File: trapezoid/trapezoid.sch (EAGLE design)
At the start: 33 parts, among them U1 MMA8452Q, U2 microSD, U4 MCP73831, Y1 CRYSTAL.ABS25

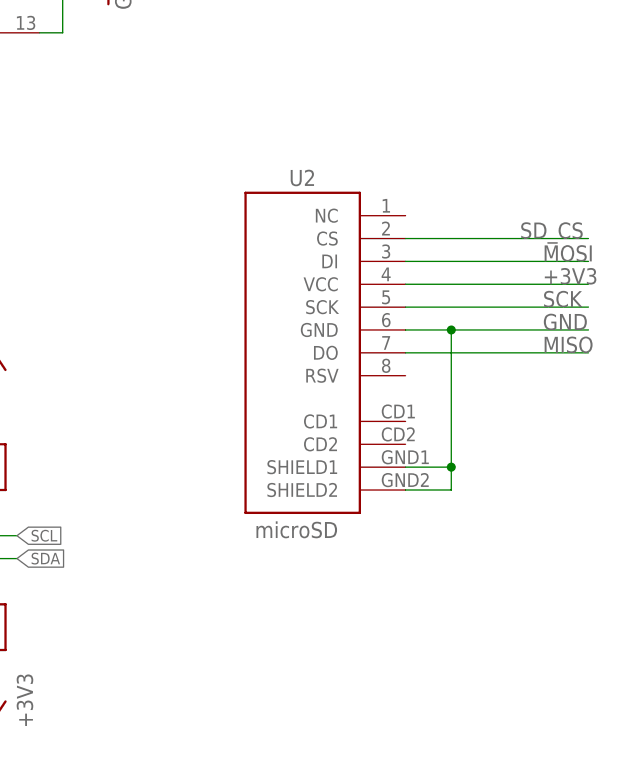
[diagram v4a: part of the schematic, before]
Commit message: put new uSD slot on board
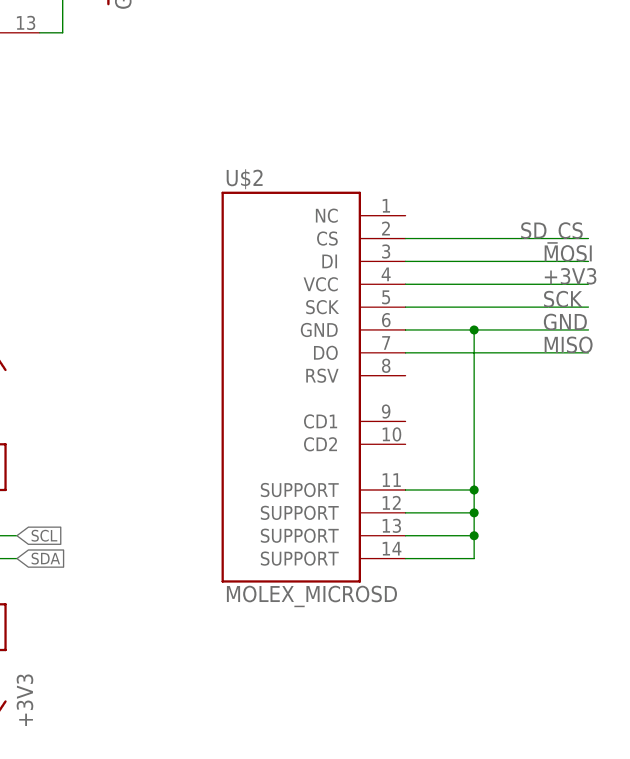
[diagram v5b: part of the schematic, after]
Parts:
- removed U2: microSD, SparkFun:USD-SOCKETSMD
- added U$2: MOLEX_MICROSD, sharkdunio:MOLEX_MICROSD
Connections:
- net +3V3: now also U$2.VCC; no longer U2.VCC
- net GND: now also U$2.GND, U$2.SUPPORT@1, U$2.SUPPORT@2, U$2.SUPPORT@3, U$2.SUPPORT@4; no longer U2.GND, U2.SHIELD1, U2.SHIELD2
- net MISO: now also U$2.DO; no longer U2.DO
- net MOSI: now also U$2.DI; no longer U2.DI
- net SCK: now also U$2.SCK; no longer U2.SCK
- net SD_CS: now also U$2.CS; no longer U2.CS
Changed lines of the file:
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@@
 <setting verticaltext="up"/>
 </settings>
-<grid distance="0.1" unitdist="inch" unit="inch" style="lines" multiple="1" display="no" altdistance="0.01" altunitdist="inch" altunit="inch"/>
+<grid distance="0.1" unitdist="inch" unit="inch" style="lines" multiple="1" display="yes" altdistance="0.01" altunitdist="inch" altunit="inch"/>
 <layers>
 <layer number="1" name="Top" color="4" fill="1" visible="no" active="no"/>
@@
 <part name="U1" library="SparkFun" deviceset="MMA8452Q" device=""/>
 <part name="GND1" library="SparkFun" deviceset="GND" device=""/>
-<part name="U2" library="SparkFun" deviceset="USD-SOCKET" device="SMD" value="microSD"/>
 <part name="J3" library="SparkFun-Connectors" deviceset="M02" device="LOCK"/>
 <part name="R2" library="microbuilder" deviceset="RESISTOR" device="0805_NOOUTLINE" value="10K"/>
@@
 <part name="J5" library="SparkFun-Connectors" deviceset="M02" device="LOCK"/>
 <part name="GND11" library="SparkFun-Aesthetics" deviceset="GND" device=""/>
+<part name="U$2" library="sharkdunio" deviceset="MOLEX_MICROSD" device=""/>
 </parts>
 <sheets>
@@
 <instance part="U1" gate="G$1" x="50.8" y="-12.7"/>
 <instance part="GND1" gate="1" x="38.1" y="-30.48"/>
-<instance part="U2" gate="G$1" x="172.72" y="5.08" smashed="yes" rot="MR0">
-<attribute name="NAME" x="167.386" y="21.082" size="1.778" layer="95"/>
-<attribute name="VALUE" x="163.576" y="-18.034" size="1.778" layer="96"/>
-</instance>
 <instance part="J3" gate="G$1" x="119.38" y="-20.32"/>
 <instance part="R2" gate="G$1" x="134.62" y="-27.94" rot="R90"/>
@@
 <instance part="J5" gate="G$1" x="5.08" y="63.5"/>
 <instance part="GND11" gate="1" x="15.24" y="58.42"/>
+<instance part="U$2" gate="G$1" x="167.64" y="-2.54"/>
 </instances>
 <busses>
@@
 </segment>
 <segment>
-<wire x1="180.34" y1="5.08" x2="185.42" y2="5.08" width="0.1524" layer="91"/>
-<wire x1="185.42" y1="5.08" x2="200.66" y2="5.08" width="0.1524" layer="91"/>
-<wire x1="180.34" y1="-12.7" x2="185.42" y2="-12.7" width="0.1524" layer="91"/>
-<wire x1="185.42" y1="-12.7" x2="185.42" y2="-10.16" width="0.1524" layer="91"/>
-<wire x1="185.42" y1="-10.16" x2="185.42" y2="5.08" width="0.1524" layer="91"/>
-<wire x1="180.34" y1="-10.16" x2="185.42" y2="-10.16" width="0.1524" layer="91"/>
-<junction x="185.42" y="5.08"/>
-<junction x="185.42" y="-10.16"/>
-<pinref part="U2" gate="G$1" pin="GND"/>
-<pinref part="U2" gate="G$1" pin="SHIELD1"/>
-<pinref part="U2" gate="G$1" pin="SHIELD2"/>
+<wire x1="180.34" y1="5.08" x2="187.96" y2="5.08" width="0.1524" layer="91"/>
 <label x="195.58" y="5.08" size="1.778" layer="95"/>
+<pinref part="U$2" gate="G$1" pin="GND"/>
+<pinref part="U$2" gate="G$1" pin="SUPPORT@4"/>
+<wire x1="187.96" y1="5.08" x2="200.66" y2="5.08" width="0.1524" layer="91"/>
+<wire x1="180.34" y1="-20.32" x2="187.96" y2="-20.32" width="0.1524" layer="91"/>
+<wire x1="187.96" y1="-20.32" x2="187.96" y2="-17.78" width="0.1524" layer="91"/>
+<junction x="187.96" y="5.08"/>
+<pinref part="U$2" gate="G$1" pin="SUPPORT@3"/>
+<wire x1="187.96" y1="-17.78" x2="187.96" y2="-15.24" width="0.1524" layer="91"/>
+<wire x1="187.96" y1="-15.24" x2="187.96" y2="-12.7" width="0.1524" layer="91"/>
+<wire x1="187.96" y1="-12.7" x2="187.96" y2="5.08" width="0.1524" layer="91"/>
+<wire x1="180.34" y1="-17.78" x2="187.96" y2="-17.78" width="0.1524" layer="91"/>
+<junction x="187.96" y="-17.78"/>
+<pinref part="U$2" gate="G$1" pin="SUPPORT@2"/>
+<wire x1="180.34" y1="-15.24" x2="187.96" y2="-15.24" width="0.1524" layer="91"/>
+<junction x="187.96" y="-15.24"/>
+<pinref part="U$2" gate="G$1" pin="SUPPORT@1"/>
+<wire x1="180.34" y1="-12.7" x2="187.96" y2="-12.7" width="0.1524" layer="91"/>
+<junction x="187.96" y="-12.7"/>
 </segment>
 <segment>
@@
 <segment>
 <wire x1="180.34" y1="15.24" x2="200.66" y2="15.24" width="0.1524" layer="91"/>
-<pinref part="U2" gate="G$1" pin="CS"/>
 <label x="193.04" y="15.24" size="1.778" layer="95"/>
+<pinref part="U$2" gate="G$1" pin="CS"/>
 </segment>
 <segment>
@@
 <segment>
 <wire x1="180.34" y1="12.7" x2="200.66" y2="12.7" width="0.1524" layer="91"/>
-<pinref part="U2" gate="G$1" pin="DI"/>
 <label x="195.58" y="12.7" size="1.778" layer="95"/>
+<pinref part="U$2" gate="G$1" pin="DI"/>
 </segment>
 <segment>
@@
 <segment>
 <wire x1="180.34" y1="7.62" x2="200.66" y2="7.62" width="0.1524" layer="91"/>
-<pinref part="U2" gate="G$1" pin="SCK"/>
 <label x="195.58" y="7.62" size="1.778" layer="95"/>
+<pinref part="U$2" gate="G$1" pin="SCK"/>
 </segment>
 <segment>
@@
 <segment>
 <wire x1="180.34" y1="2.54" x2="200.66" y2="2.54" width="0.1524" layer="91"/>
-<pinref part="U2" gate="G$1" pin="DO"/>
 <label x="195.58" y="2.54" size="1.778" layer="95"/>
+<pinref part="U$2" gate="G$1" pin="DO"/>
 </segment>
 <segment>
@@
 <segment>
 <wire x1="180.34" y1="10.16" x2="200.66" y2="10.16" width="0.1524" layer="91"/>
-<pinref part="U2" gate="G$1" pin="VCC"/>
 <label x="195.58" y="10.16" size="1.778" layer="95"/>
-</segment>
-<segment>
+<pinref part="U$2" gate="G$1" pin="VCC"/>
+</segment>
+<segment>

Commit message: silk
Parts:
- C6: value 0.1uF -> 1.0uF
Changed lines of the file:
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@@
 <setting verticaltext="up"/>
 </settings>
-<grid distance="0.1" unitdist="inch" unit="inch" style="lines" multiple="1" display="yes" altdistance="0.01" altunitdist="inch" altunit="inch"/>
+<grid distance="0.1" unitdist="inch" unit="inch" style="lines" multiple="1" display="no" altdistance="0.01" altunitdist="inch" altunit="inch"/>
 <layers>
 <layer number="1" name="Top" color="4" fill="1" visible="no" active="no"/>
@@
 <part name="C4" library="microbuilder" deviceset="CAP_CERAMIC" device="0805-NOOUTLINE" value="0.1uF"/>
 <part name="C5" library="microbuilder" deviceset="CAP_CERAMIC" device="0805-NOOUTLINE" value="0.1uF"/>
-<part name="C6" library="microbuilder" deviceset="CAP_CERAMIC" device="0805-NOOUTLINE" value="0.1uF"/>
+<part name="C6" library="microbuilder" deviceset="CAP_CERAMIC" device="0805-NOOUTLINE" value="1.0uF"/>
 <part name="J5" library="SparkFun-Connectors" deviceset="M02" device="LOCK"/>
 <part name="GND11" library="SparkFun-Aesthetics" deviceset="GND" device=""/>

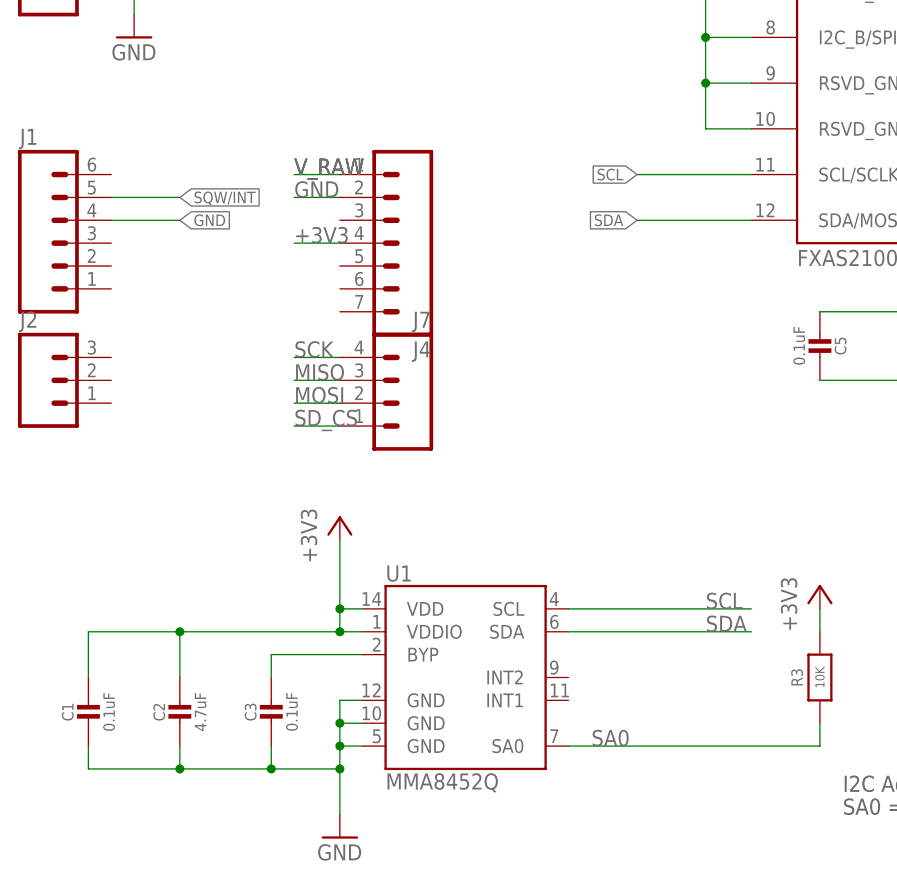
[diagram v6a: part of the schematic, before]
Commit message: broke out accel int
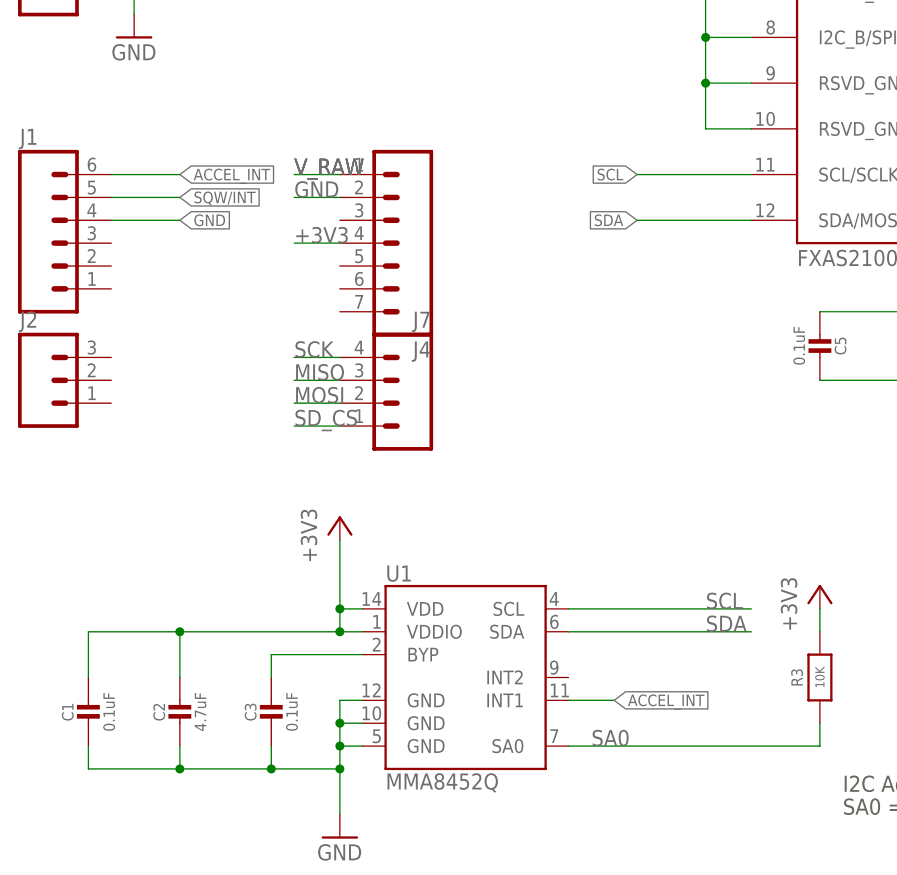
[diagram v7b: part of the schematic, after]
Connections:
- new net ACCEL_INT: J1.6, U1.INT1
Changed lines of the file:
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@@
+</segment>
+</net>
+<net name="ACCEL_INT" class="0">
+<segment>
+<pinref part="U1" gate="G$1" pin="INT1"/>
+<wire x1="63.5" y1="-15.24" x2="68.58" y2="-15.24" width="0.1524" layer="91"/>
+<label x="68.58" y="-15.24" size="1.27" layer="95" xref="yes"/>
+</segment>
+<segment>
+<pinref part="J1" gate="G$1" pin="6"/>
+<wire x1="12.7" y1="43.18" x2="20.32" y2="43.18" width="0.1524" layer="91"/>
+<label x="20.32" y="43.18" size="1.27" layer="95" xref="yes"/>
 </segment>
 </net>

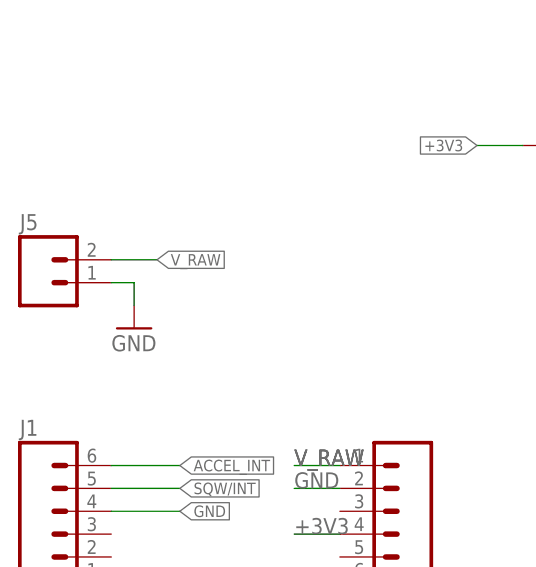
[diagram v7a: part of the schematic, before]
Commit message: fixed external power headers
conected external power headers to unrgulated side of rulgulator
instead of regulated
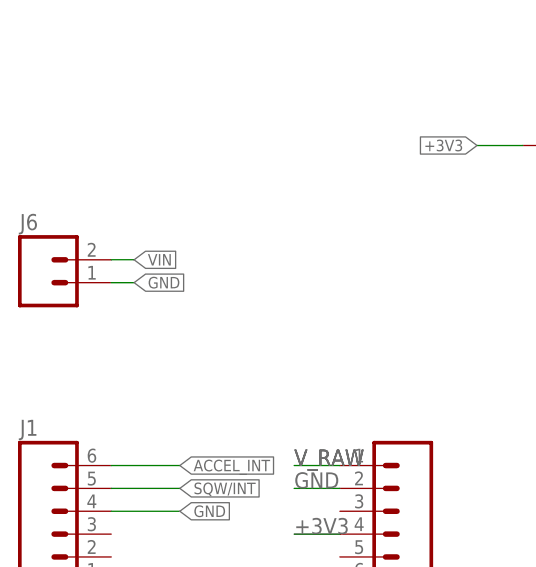
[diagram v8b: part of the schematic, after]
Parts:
- renumbered J5 to J6
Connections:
- net VIN: now also J6.2
- net V_RAW: no longer J6.2
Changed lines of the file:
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@@
 <part name="C5" library="microbuilder" deviceset="CAP_CERAMIC" device="0805-NOOUTLINE" value="0.1uF"/>
 <part name="C6" library="microbuilder" deviceset="CAP_CERAMIC" device="0805-NOOUTLINE" value="1.0uF"/>
-<part name="J5" library="SparkFun-Connectors" deviceset="M02" device="LOCK"/>
-<part name="GND11" library="SparkFun-Aesthetics" deviceset="GND" device=""/>
 <part name="U$2" library="sharkdunio" deviceset="MOLEX_MICROSD" device=""/>
+<part name="J6" library="SparkFun-Connectors" deviceset="M02" device="LOCK"/>
 </parts>
 <sheets>
@@
 <instance part="C5" gate="G$1" x="91.44" y="25.4" rot="R180"/>
 <instance part="C6" gate="G$1" x="106.68" y="25.4" rot="R180"/>
-<instance part="J5" gate="G$1" x="5.08" y="63.5"/>
-<instance part="GND11" gate="1" x="15.24" y="58.42"/>
 <instance part="U$2" gate="G$1" x="167.64" y="-2.54"/>
+<instance part="J6" gate="G$1" x="5.08" y="63.5"/>
 </instances>
 <busses>
@@
 </segment>
 <segment>
-<pinref part="J5" gate="G$1" pin="1"/>
+<pinref part="J6" gate="G$1" pin="1"/>
 <wire x1="12.7" y1="63.5" x2="15.24" y2="63.5" width="0.1524" layer="91"/>
-<pinref part="GND11" gate="1" pin="GND"/>
-<wire x1="15.24" y1="63.5" x2="15.24" y2="60.96" width="0.1524" layer="91"/>
+<label x="15.24" y="63.5" size="1.27" layer="95" xref="yes"/>
 </segment>
 </net>
@@
 <pinref part="JP1" gate="G$1" pin="+"/>
 <pinref part="C8" gate="G$1" pin="1"/>
-</segment>
-<segment>
-<pinref part="J5" gate="G$1" pin="2"/>
-<wire x1="12.7" y1="66.04" x2="17.78" y2="66.04" width="0.1524" layer="91"/>
-<label x="17.78" y="66.04" size="1.27" layer="95" xref="yes"/>
 </segment>
 </net>
@@
 <pinref part="C7" gate="G$1" pin="1"/>
 </segment>
-</net>
+<segment>
+<pinref part="J6" gate="G$1" pin="2"/>
+<wire x1="12.7" y1="66.04" x2="15.24" y2="66.04" width="0.1524" layer="91"/>
+<label x="15.24" y="66.04" size="1.27" layer="95" xref="yes"/>
+</segment>
+</net>
